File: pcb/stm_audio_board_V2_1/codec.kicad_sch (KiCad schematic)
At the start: 15 parts, among them Y1 Crystal_GND24

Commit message: fixes in pcb
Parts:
- C38: value 5.6nF -> 39nF
- C39: value 390pF -> 2.2nF
- R12: value 562 -> 3.32k
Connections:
- net +3.3VA: now also C39.1, R12.2
- net GND: no longer C39.1, R12.2

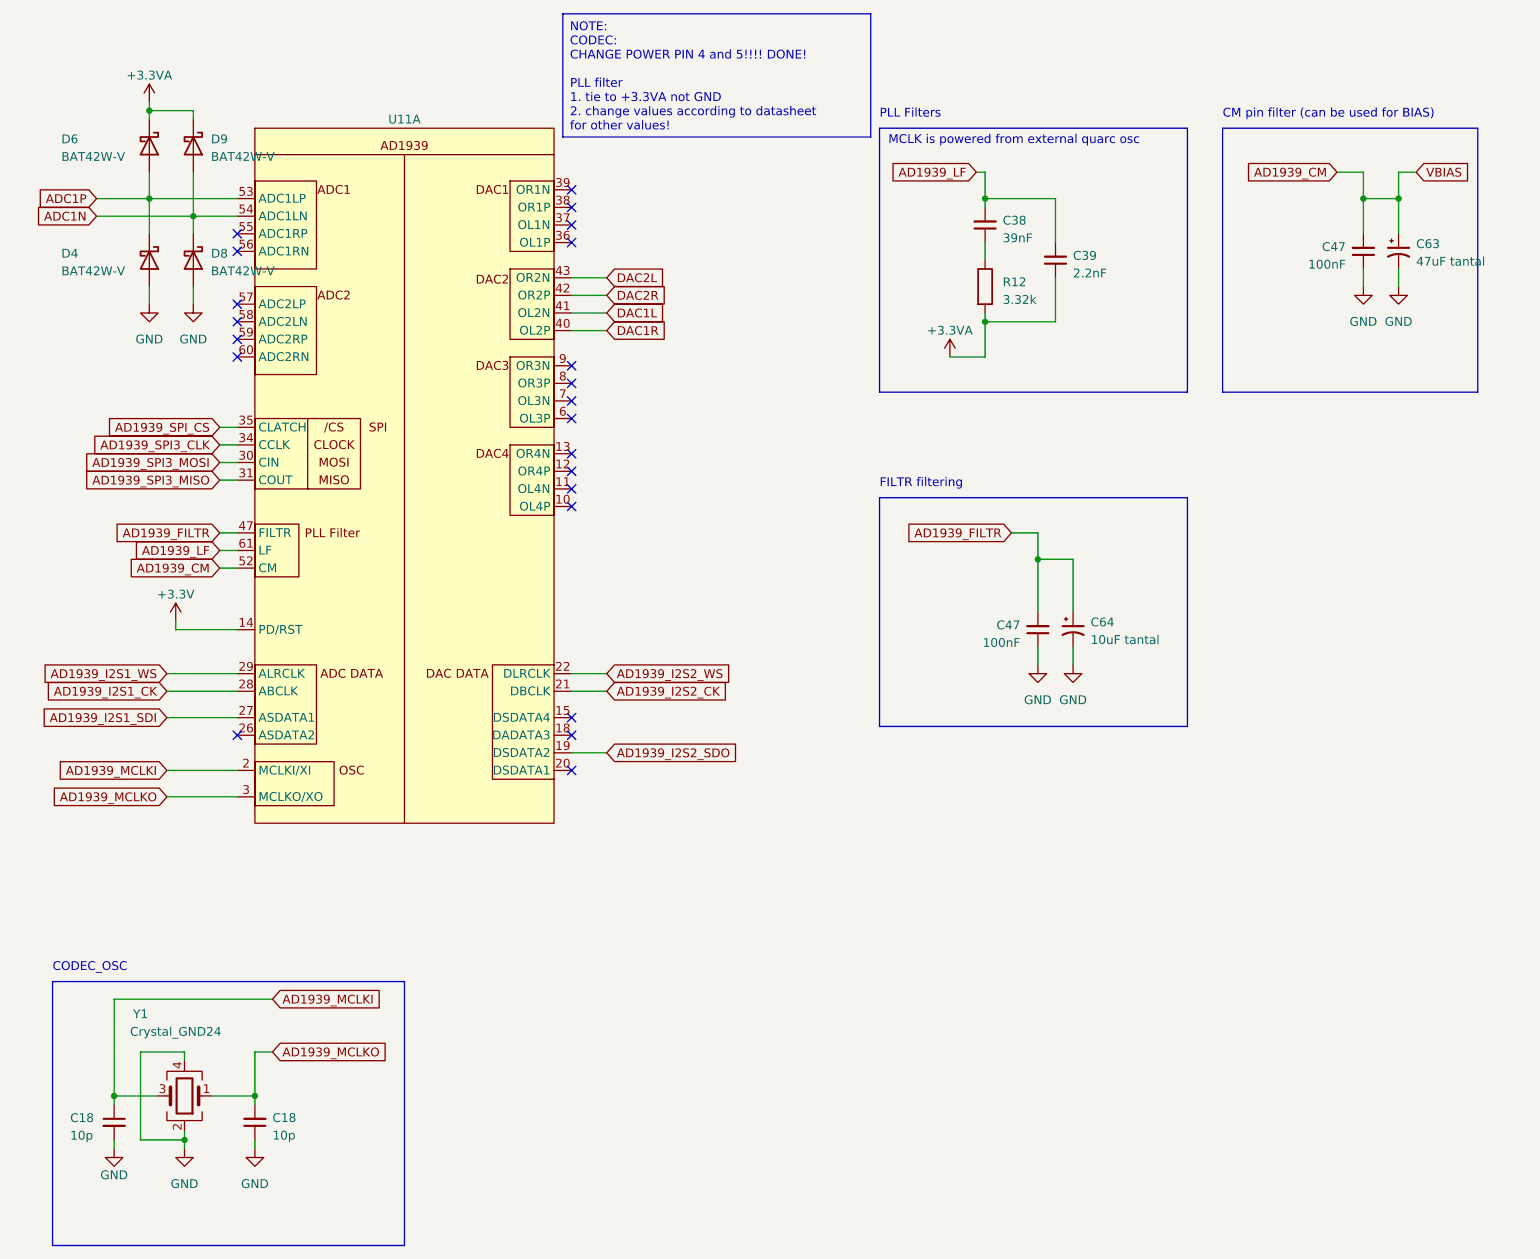
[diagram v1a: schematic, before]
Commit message: audo_board v2_1 output stage is reworked
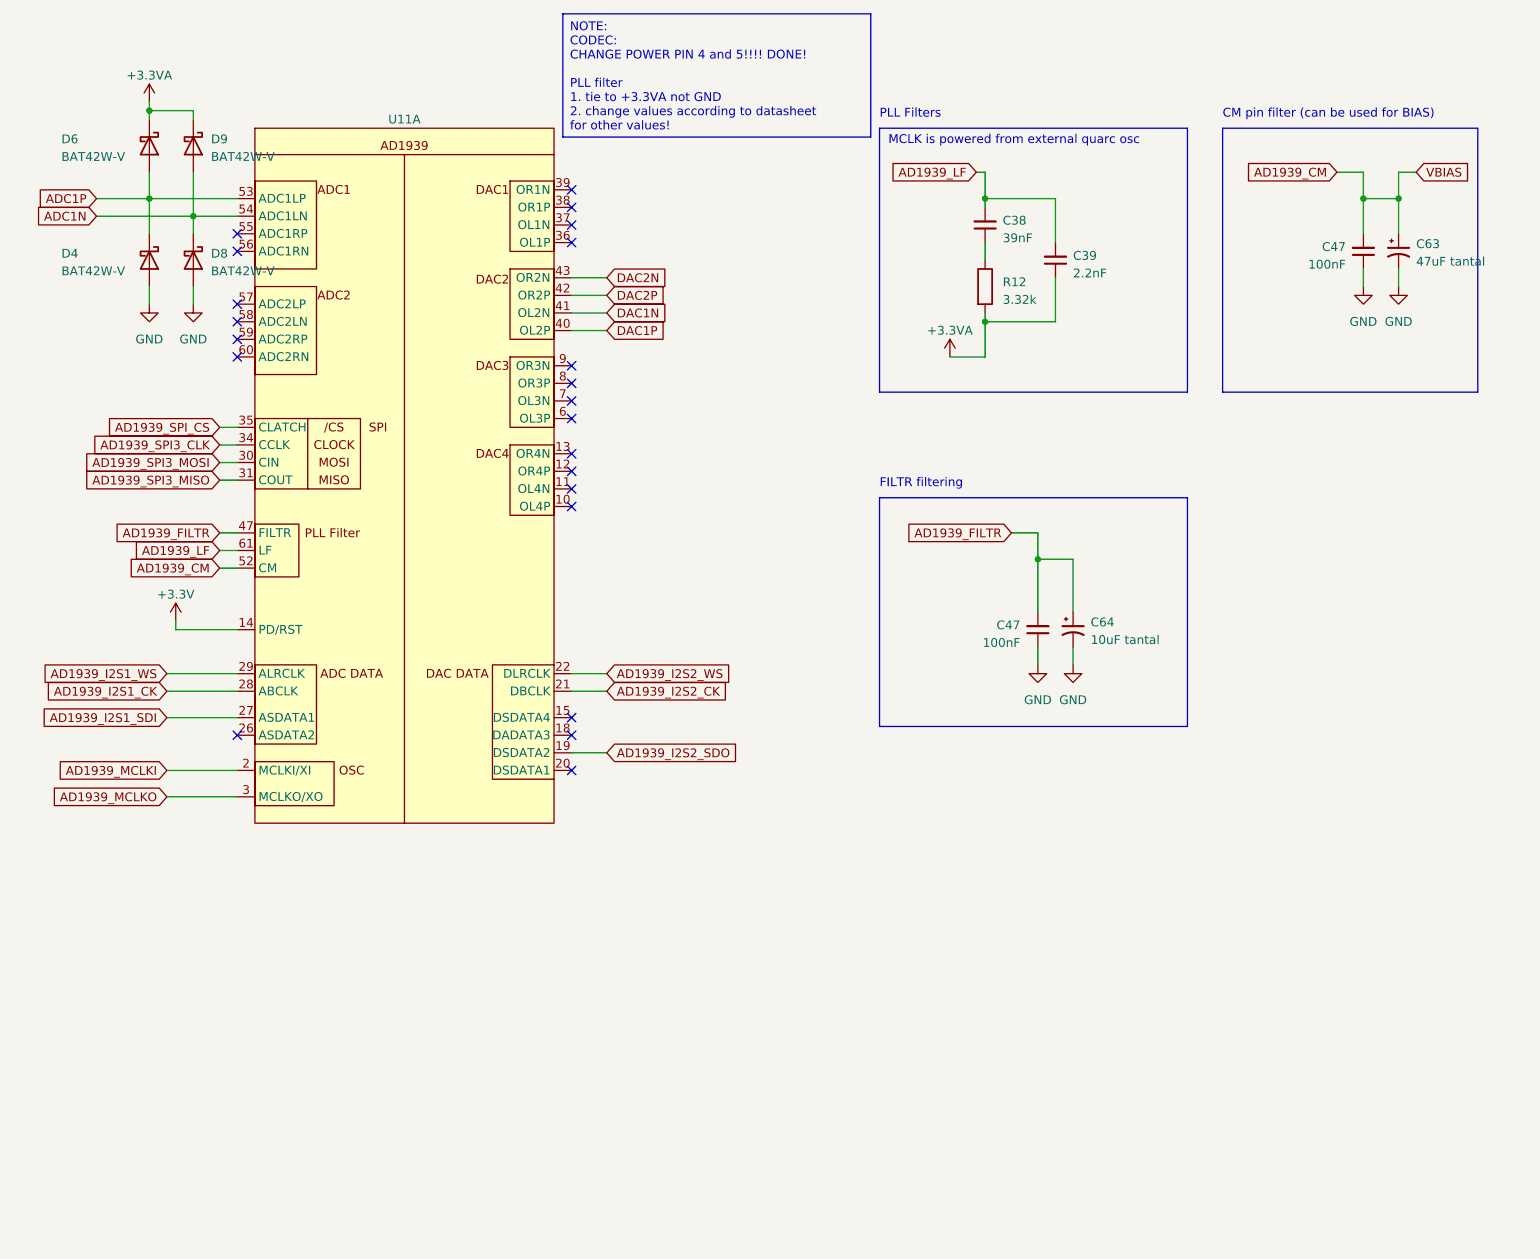
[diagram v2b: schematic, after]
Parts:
- removed C18 (x2): 10p, Capacitor_SMD:C_0603_1608Metric_Pad1.08x0.95mm_HandSolder, symbol Device:C_Small
- removed Y1: Crystal_GND24, Crystal:Crystal_SMD_5032-4Pin_5.0x3.2mm, symbol Device:Crystal_GND24
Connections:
- net DAC1L renamed DAC1N
- net DAC1R renamed DAC1P
- net DAC2L renamed DAC2N
- net DAC2R renamed DAC2P
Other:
- note removed: "CODEC_OSC"
